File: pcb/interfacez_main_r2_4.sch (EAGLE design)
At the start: 169 parts, among them IC1 STMPS2141STR, IC10 74LCX245FT, IC11 74LCX245FT, IC12 USB1T11AMTCX, IC13 74LVC06APW,118, IC2 EP4CE6E22C8N, IC3 74LCX245FT, IC4 74LCX245FT, IC5 MP2233DJ, IC6 MP2233DJ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

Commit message: Add r2.4 mainboard files
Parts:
- removed R1: 10K, GadgetFactory:R0603
- removed SD1: 1040310811, alvie:1040310811
- added T+12V, T+1V2, T+2V5, T+3V3, T+5V, T+9V, TP5: TPTP12SQ, testpad:TPTP12SQ
- TP4: value TPTP08R -> TPPAD1-13; device testpad:TPTP08R -> testpad:TPPAD1-13
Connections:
- removed net N$1: IC2.__IO_6/FLASH_NCS/NCSO, TP4.TP
- removed net SDMMC_DET: R1A.2, SD1.A, U1.IO17
- new net IO6: IC2.__IO_6/FLASH_NCS/NCSO, U1.IO17
- net +12V: now also T+12V.TP
- net +1V2: now also T+1V2.TP
- net +2V5: now also T+2V5.TP
- net +3V3: now also J2.VDD, T+3V3.TP; no longer R1A.1, SD1.VDD
- net +5V: now also T+5V.TP
- net +9V: now also T+9V.TP
- net GND: now also J2.VSS, TP4.TP; no longer SD1.B, SD1.S1, SD1.S2, SD1.S3, SD1.S4, SD1.VSS
- net PE: now also J2.SHIELD
- net SDMMC_CK: now also J2.CLK; no longer SD1.CLK(SCLK)
- net SDMMC_CMD: now also J2.CMD; no longer SD1.CMD(DI)
- net SDMMC_D0: now also J2.DAT0; no longer SD1.DAT0(DO)
- net SDMMC_D1: now also J2.DAT1; no longer SD1.DAT1
- net SDMMC_D2: now also J2.DAT2; no longer SD1.DAT2
- net SDMMC_D3: now also J2.CD/DAT3^2; no longer SD1.CD/DAT3(!CS!)
- net VSWITCH: now also TP5.TP
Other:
- moved on the sheet: J2, R30, TP4

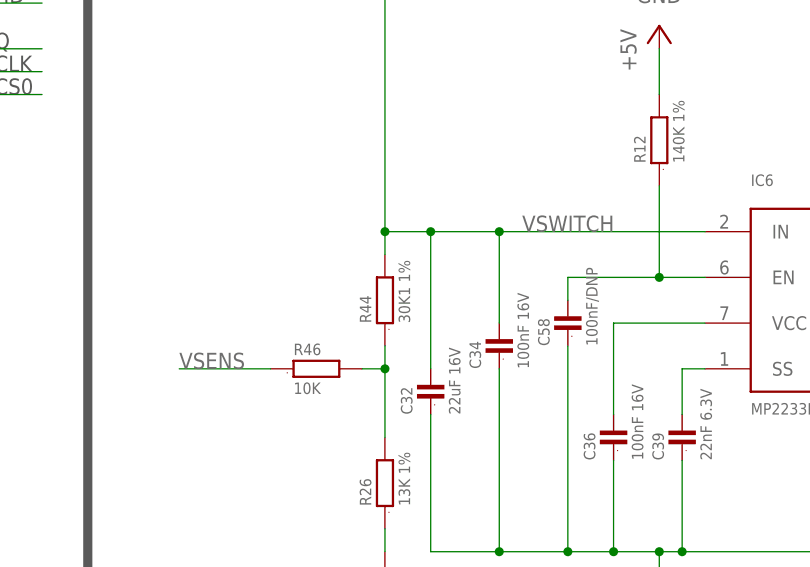
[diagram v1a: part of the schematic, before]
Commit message: pcb: fix R44 value for voltage divider
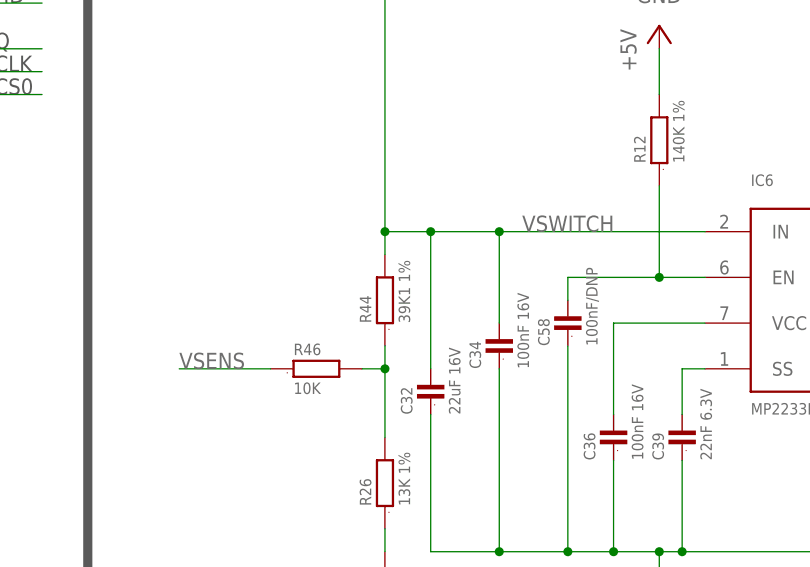
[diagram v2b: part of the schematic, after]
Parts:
- R44: value 30K1 1% -> 39K1 1%
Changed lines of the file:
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@@
 <part name="Q1" library="transistor-small-signal" deviceset="BSS123" device=""/>
 <part name="R26" library="GadgetFactory" deviceset="R" device="0603" value="13K 1%"/>
-<part name="R44" library="GadgetFactory" deviceset="R" device="0603" value="30K1 1%"/>
+<part name="R44" library="GadgetFactory" deviceset="R" device="0603" value="39K1 1%"/>
 <part name="GND42" library="supply1" deviceset="GND" device=""/>
 <part name="R46" library="GadgetFactory" deviceset="R" device="0603" value="10K"/>
